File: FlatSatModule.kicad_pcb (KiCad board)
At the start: 4 copper layers, 110.2 x 119.4 mm, 8 parts, among them J1 DB26_Male_HighDensity_Mountin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, J2 Micro_SD_Card_Det, J3 HEADER_13x2

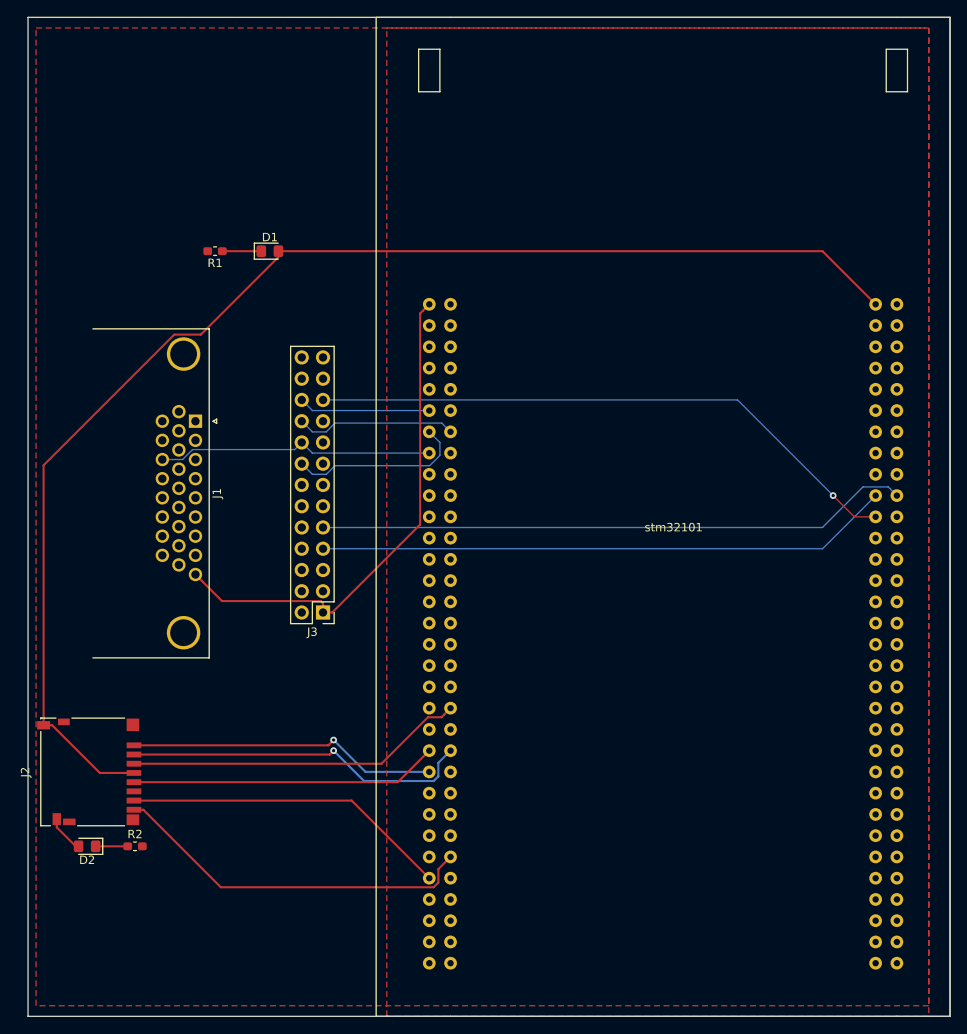
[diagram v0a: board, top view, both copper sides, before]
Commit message: Added silkscreen text
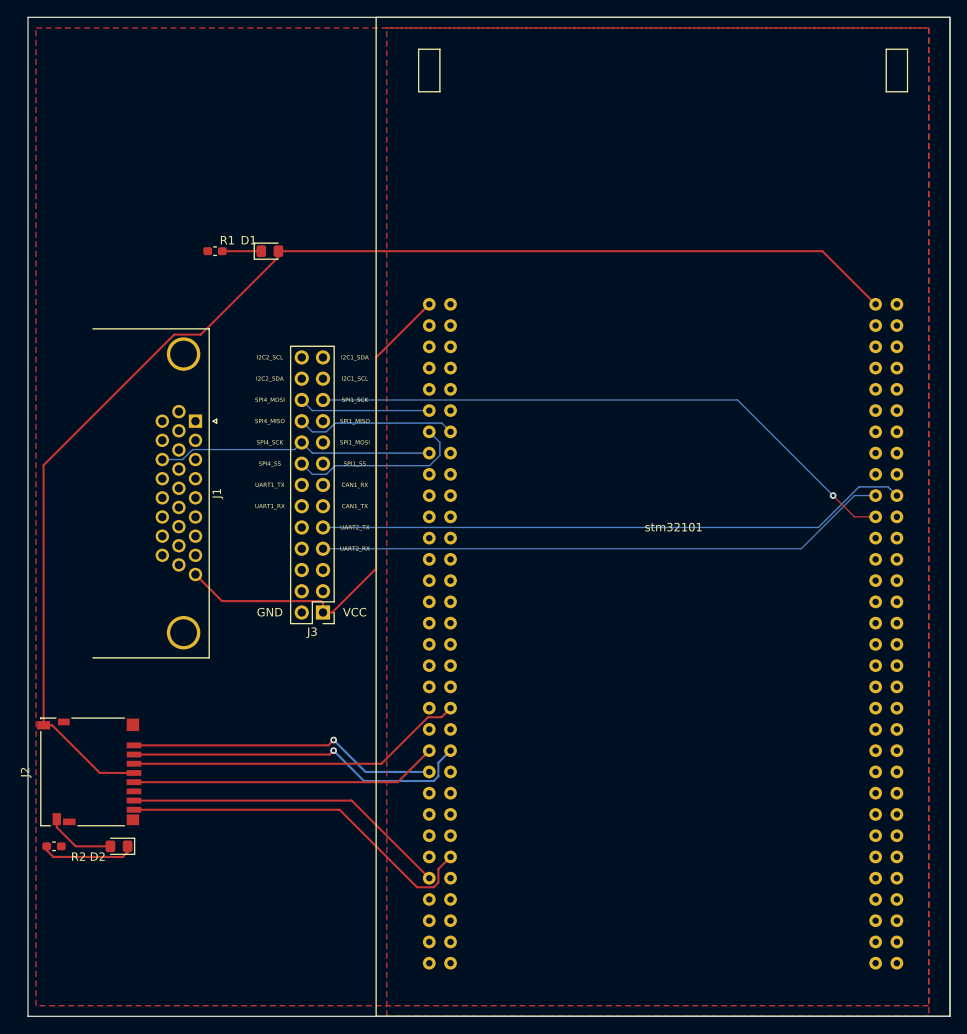
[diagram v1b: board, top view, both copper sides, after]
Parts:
- moved R2 9.68 mm to (63.1, 127.0)
- moved D2 3.81 mm to (70.9, 127.0)
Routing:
- net Net-(D2-Pad1): track 3.82 -> 11.4 mm
- net /SD_DET: track 4.52 -> 8.33 mm
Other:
- board text added: "CAN1_RX"
- board text added: "CAN1_TX"
- board text added: "GND"
- board text added: "I2C1_SCL"
- board text added: "I2C1_SDA"
- board text added: "I2C2_SCL"
- board text added: "I2C2_SDA"
- board text added: "SPI1_MISO"
- board text added: "SPI1_MOSI"
- board text added: "SPI1_SCK"
- board text added: "SPI1_SS"
- board text added: "SPI4_MISO"
- board text added: "SPI4_MOSI"
- board text added: "SPI4_SCK"
- board text added: "SPI4_SS"
- board text added: "UART1_RX"
- board text added: "UART1_TX"
- board text added: "UART2_RX"
- board text added: "UART2_TX"
- board text added: "VCC"
